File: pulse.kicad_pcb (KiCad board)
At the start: 2 copper layers, 93.7 x 37.9 mm, 85 parts, among them J1 D-, J10 OUT_12V, J11 OUT_24V, J12 OUT_5V, J13 USB4085-GF-A_REVA, J2 D+, J3 OUT_VUSB, J4 Conn_01x05_Male, J5 EN_3v3, J6 EN_5V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

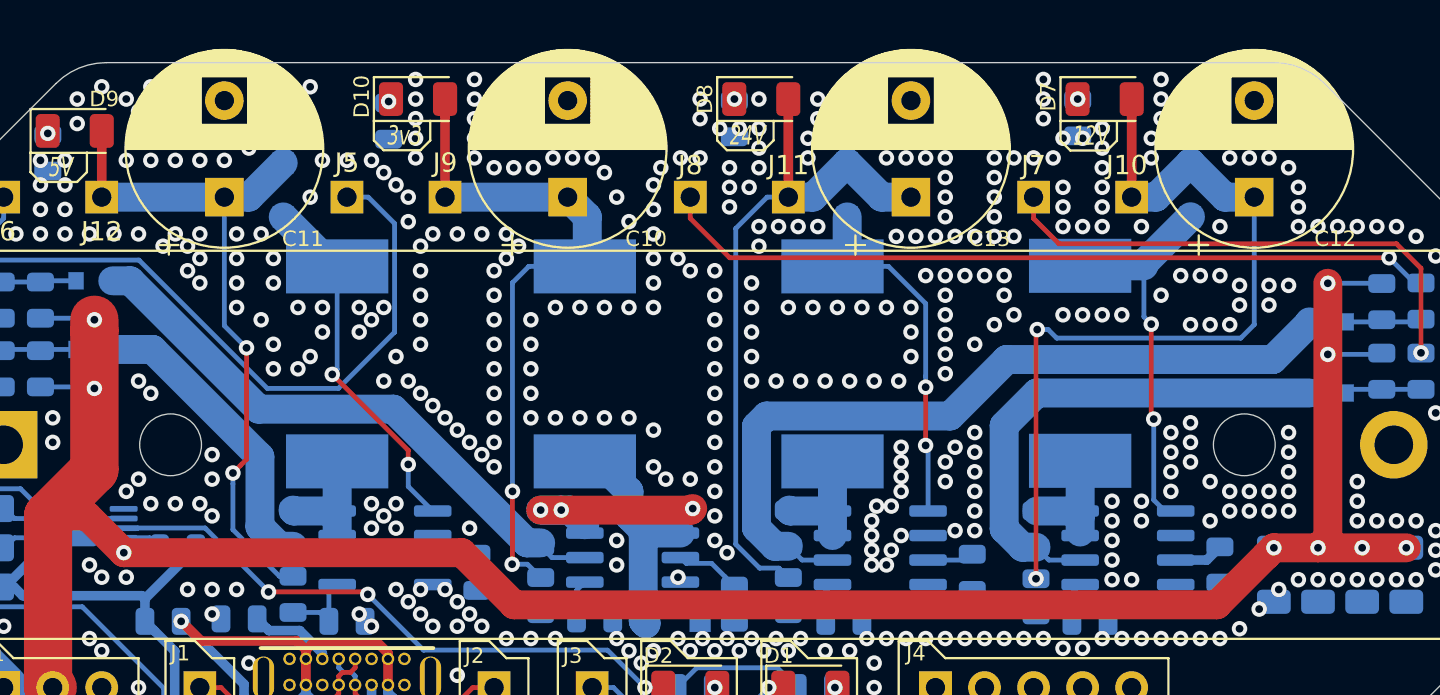
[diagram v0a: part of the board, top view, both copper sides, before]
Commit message: Fix inductor footprint and routing
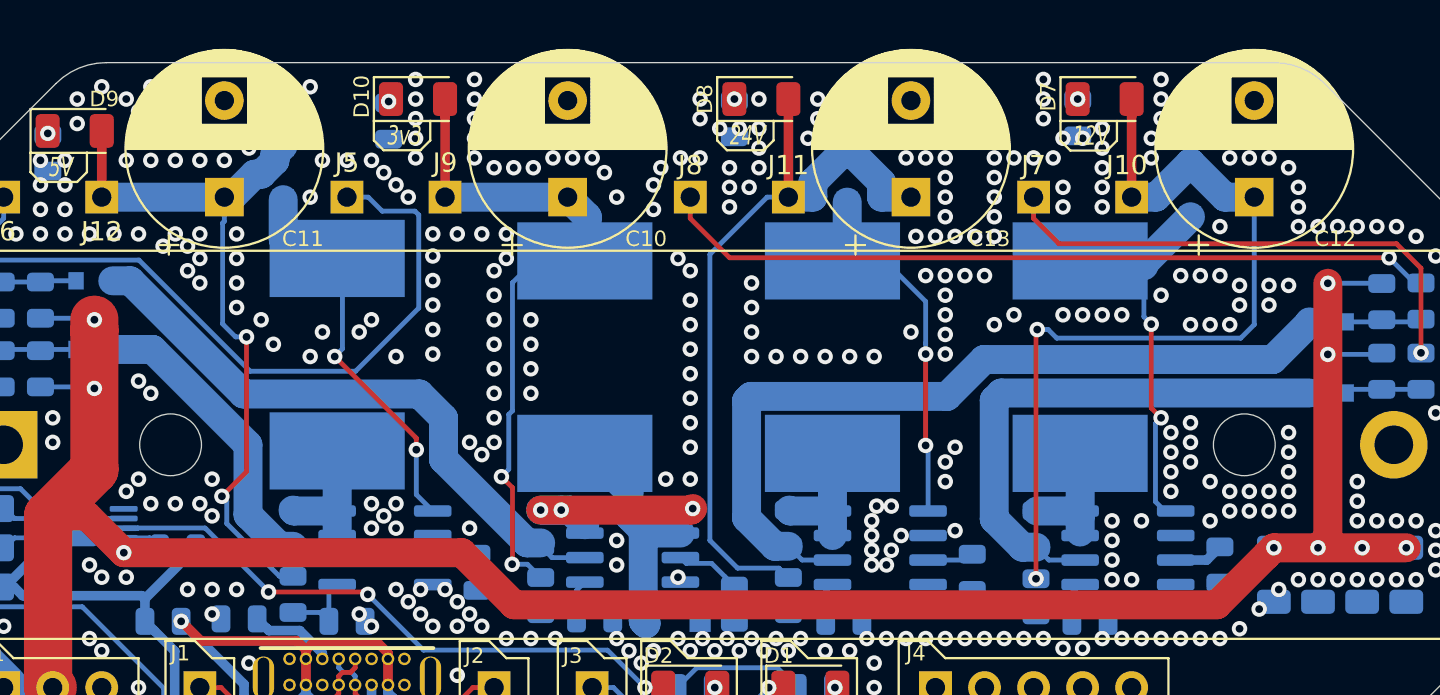
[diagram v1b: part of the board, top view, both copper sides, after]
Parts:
- L1, L2, L3, L4: footprint isomorph:L_Bourns_SRR1210A_3D -> isomorph:L_Bourns_SRR1208
- moved D4 0.89 mm to (131.3, 47.0)
- moved D6 0.77 mm to (160.5, 47.1)
- moved L1 0.51 mm to (134.1, 56.4)
- moved L3 0.38 mm to (159.8, 56.5)
- moved L4 0.38 mm to (146.9, 56.5)
- moved L2 0.35 mm to (172.6, 56.5)
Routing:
- net Net-(C13-Pad1): track 36.1 -> 39.4 mm
- net Net-(D4-Pad2): track 19.0 -> 20.8 mm
- net Net-(Q3-Pad2): track 26.5 -> 28.0 mm
- net Net-(Q4-Pad2): track 40.8 -> 42.3 mm
- net Net-(C11-Pad1): track 35.7 -> 37.1 mm
- net Net-(J5-Pad1): track 37.1 -> 38.4 mm
- net Net-(Q1-Pad2): track 30.3 -> 31.6 mm
- net Net-(D6-Pad2): track 19.3 -> 20.1 mm
- net GND: vias 482 -> 398
- net (no net): vias 1 -> 0

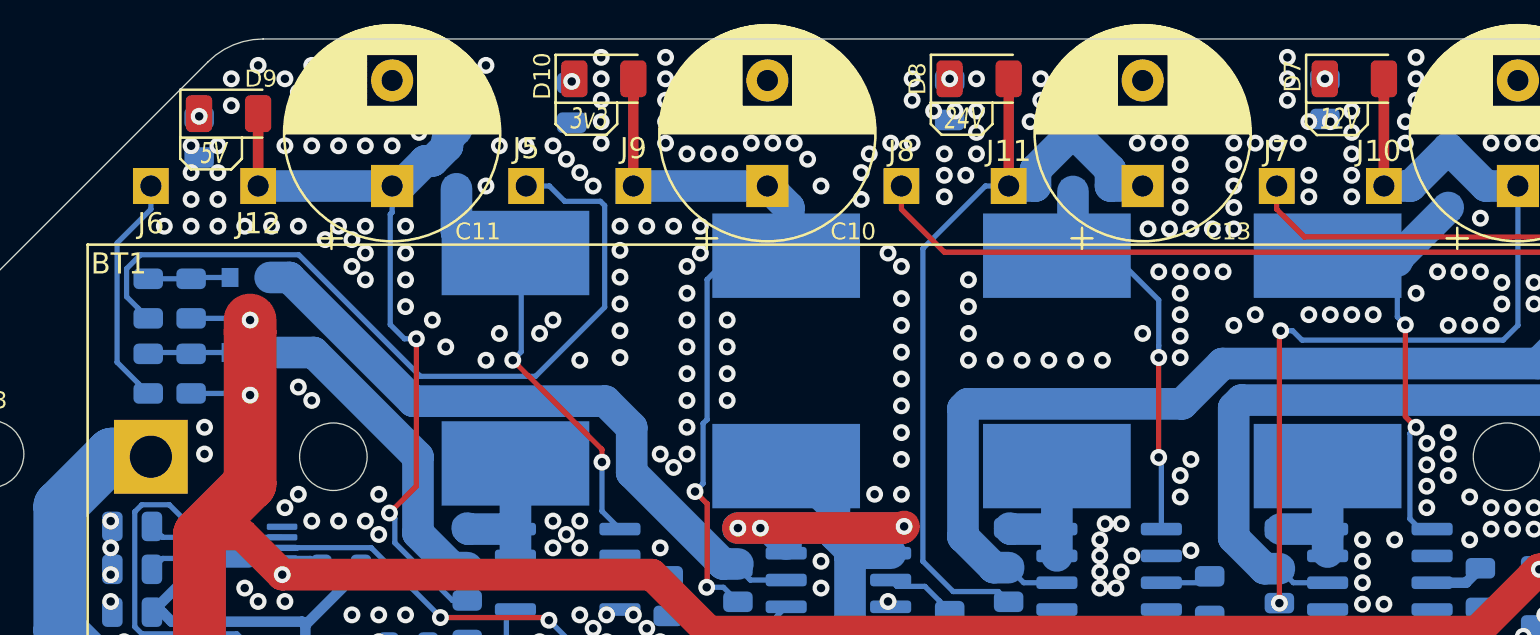
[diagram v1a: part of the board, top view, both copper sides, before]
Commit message: Fix bottom silkscreen and inductor alignment
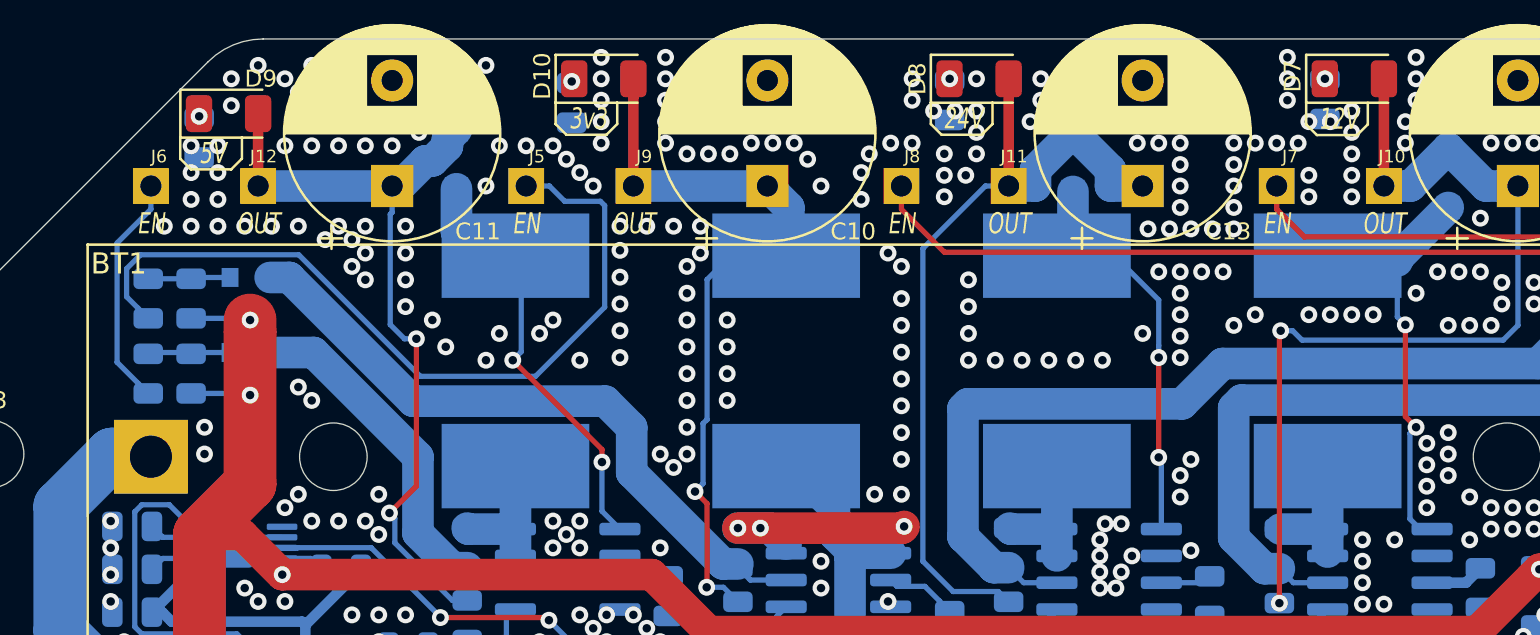
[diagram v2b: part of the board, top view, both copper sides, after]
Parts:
- moved L1 0.13 mm to (134.1, 56.5)
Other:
- board text added: "EN"
- board text added: "OUT"

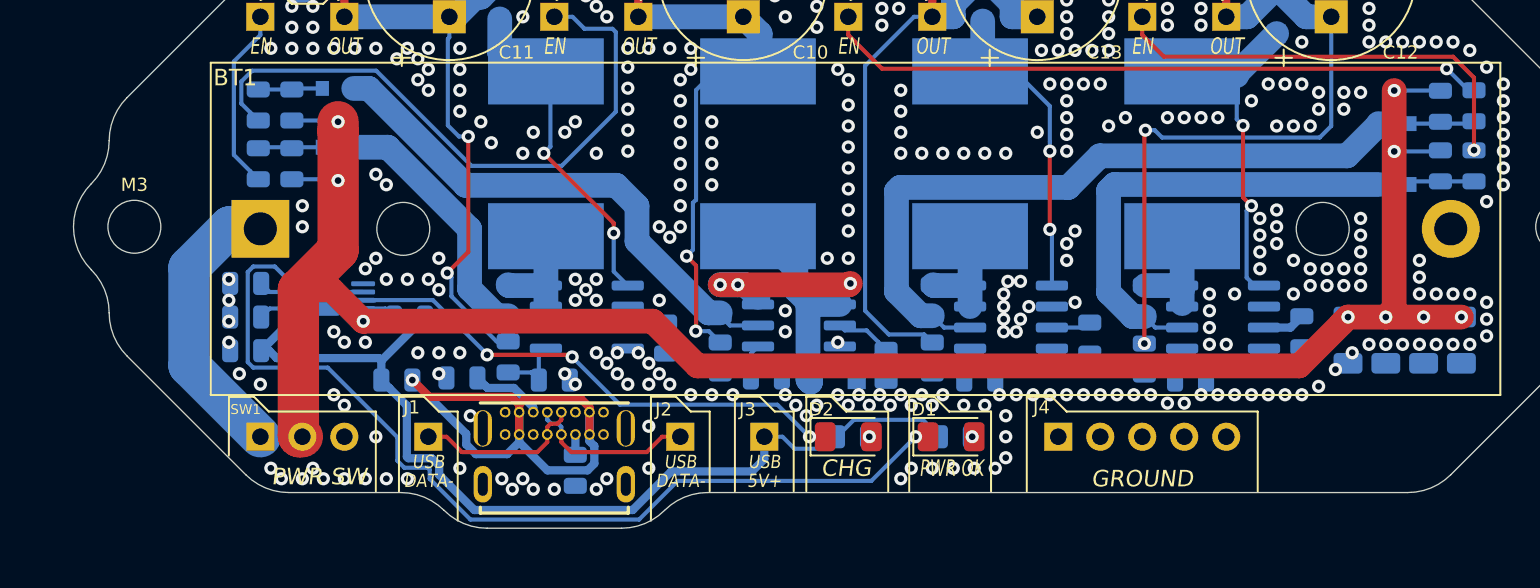
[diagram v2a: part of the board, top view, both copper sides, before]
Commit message: Add logos to silkscreen
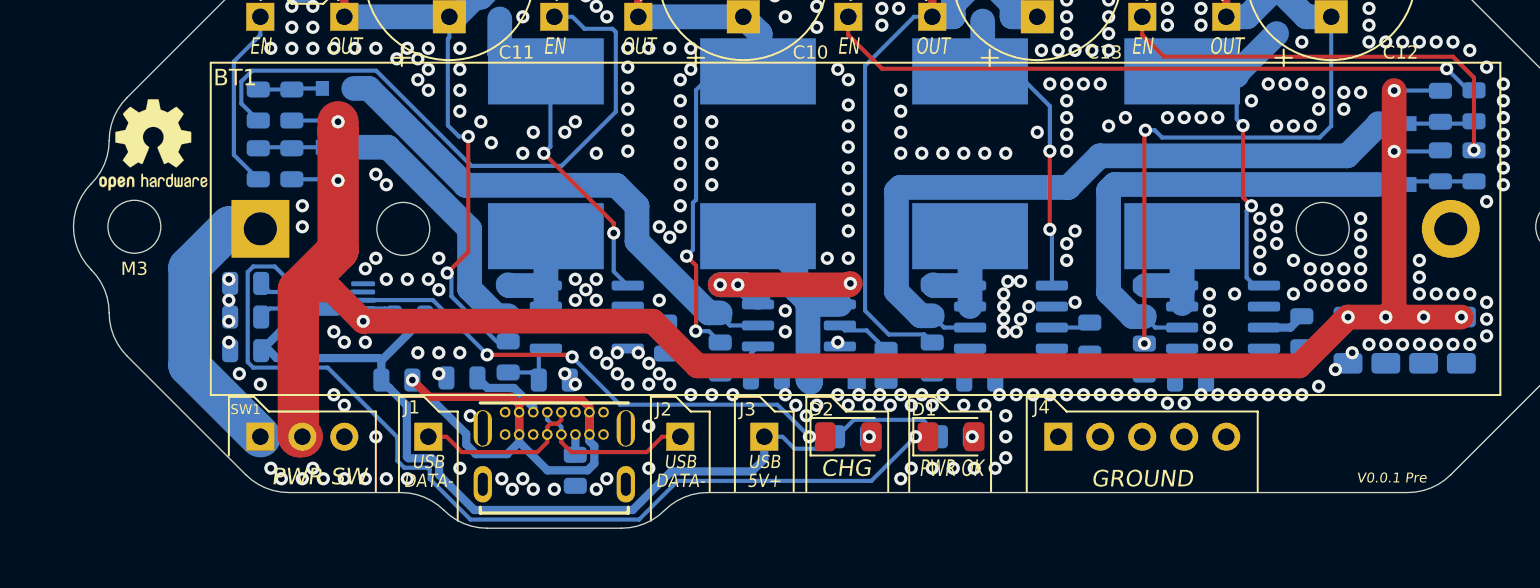
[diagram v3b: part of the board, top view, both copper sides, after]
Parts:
- added G***: LOGO, isomorph:pulse-logo-mask, F.Cu at (182.9, 73.7)
- added REF**: OSHW-Logo2_7.3x6mm_SilkScreen, Symbol:OSHW-Logo2_7.3x6mm_SilkScreen, F.Cu at (110.4, 56.0)
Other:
- board text added: "V0.0.1 Pre"
- board text added: "https://github.com/isomorph-research/pulse"
